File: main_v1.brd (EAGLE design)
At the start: 79.4 x 80.6 mm, 38 parts, among them IC1 MEGA8-P, IC2 7805TV, IC4 MC33063/MC34063P, IC5 MAX6921, IC6 MAX6921

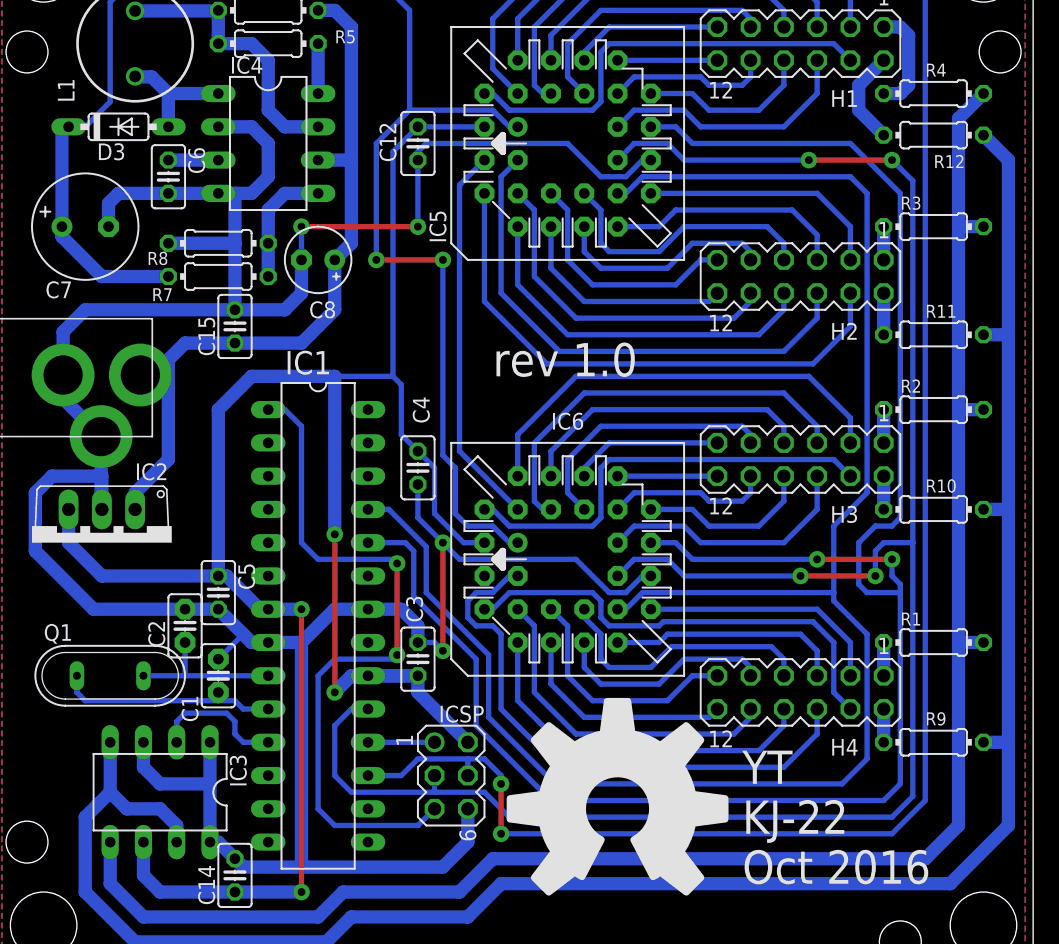
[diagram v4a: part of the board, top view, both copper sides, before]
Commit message: WIP Add a header for future expansion
Possible network connectivity, not sure how this is supposed to work
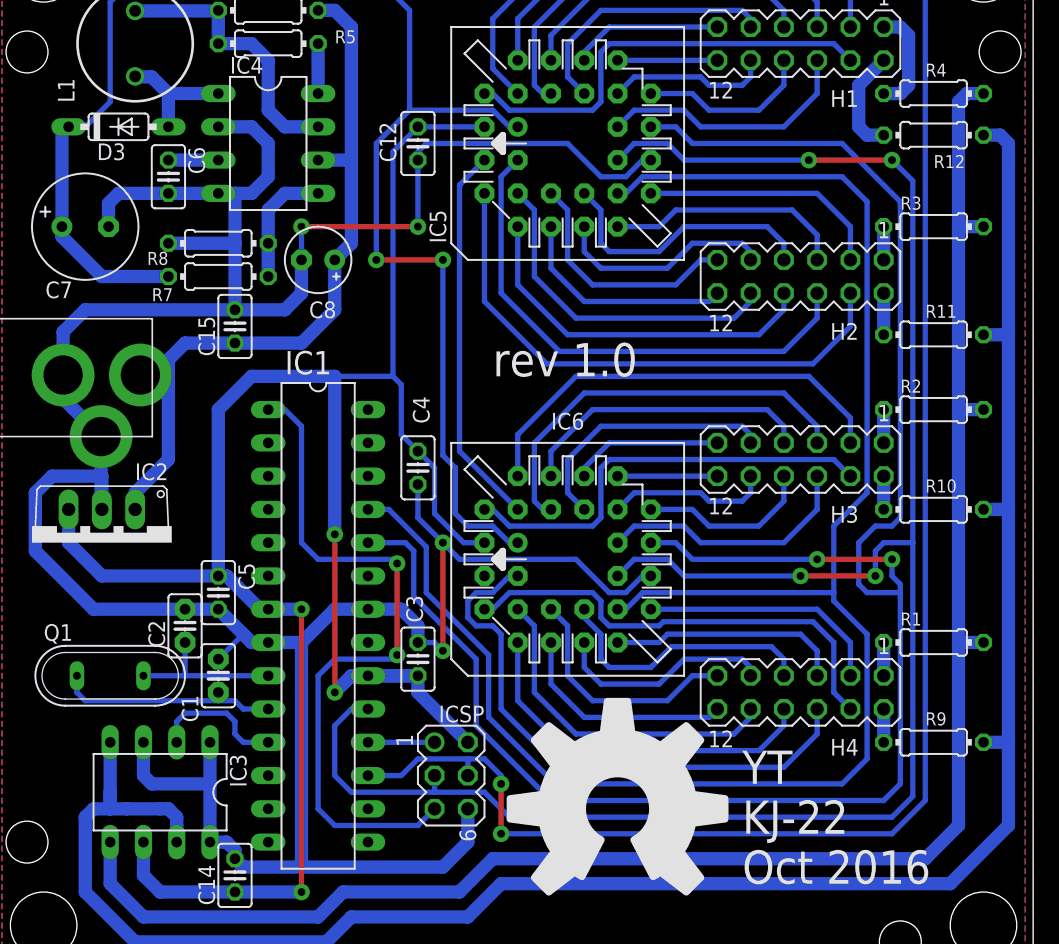
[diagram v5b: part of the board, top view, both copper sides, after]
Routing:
- net HT-: track 154.6 -> 157.2 mm
- net GND: track 249.1 -> 249.9 mm
- net HT-1: track 7.29 -> 8.04 mm
- net HT+: track 134.3 -> 135.0 mm
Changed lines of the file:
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@@
 <wire x1="26.035" y1="8.255" x2="21.59" y2="8.255" width="1.016" layer="16"/>
 <wire x1="21.59" y1="8.255" x2="20.955" y2="8.89" width="1.016" layer="16"/>
-<wire x1="20.955" y1="8.89" x2="19.685" y2="10.16" width="1.016" layer="16"/>
-<wire x1="19.685" y1="10.16" x2="19.05" y2="10.16" width="1.016" layer="16"/>
+<wire x1="20.955" y1="8.89" x2="20.955" y2="9.525" width="1.016" layer="16"/>
+<wire x1="20.955" y1="9.525" x2="20.32" y2="10.16" width="1.016" layer="16"/>
+<wire x1="20.32" y1="10.16" x2="19.05" y2="10.16" width="1.016" layer="16"/>
 <wire x1="19.05" y1="10.16" x2="19.05" y2="14.605" width="1.016" layer="16"/>
-<wire x1="19.05" y1="14.605" x2="15.24" y2="14.605" width="1.016" layer="16"/>
-<wire x1="15.24" y1="14.605" x2="13.97" y2="15.875" width="1.016" layer="16"/>
-<wire x1="13.97" y1="15.875" x2="13.97" y2="17.78" width="1.016" layer="16"/>
+<wire x1="19.05" y1="14.605" x2="14.605" y2="14.605" width="1.016" layer="16"/>
+<wire x1="14.605" y1="14.605" x2="13.97" y2="15.24" width="1.016" layer="16"/>
+<wire x1="13.97" y1="15.24" x2="13.97" y2="17.78" width="1.016" layer="16"/>
 <wire x1="19.05" y1="17.78" x2="19.05" y2="14.605" width="1.016" layer="16"/>
 <polygon width="0.4064" layer="16" spacing="10.16" isolate="1.016">
@@
 <wire x1="50.165" y1="59.69" x2="50.8" y2="59.69" width="0.4064" layer="16"/>
 <wire x1="50.8" y1="59.69" x2="52.07" y2="60.96" width="0.4064" layer="16"/>
-<wire x1="52.07" y1="60.96" x2="67.945" y2="60.96" width="0.4064" layer="16"/>
-<wire x1="67.945" y1="60.96" x2="69.215" y2="59.69" width="0.4064" layer="16"/>
-<wire x1="69.215" y1="59.69" x2="69.215" y2="36.83" width="0.4064" layer="16"/>
+<wire x1="52.07" y1="60.96" x2="67.31" y2="60.96" width="0.4064" layer="16"/>
+<wire x1="67.31" y1="60.96" x2="69.215" y2="59.055" width="0.4064" layer="16"/>
+<wire x1="69.215" y1="59.055" x2="69.215" y2="36.83" width="0.4064" layer="16"/>
 <wire x1="69.215" y1="36.83" x2="66.675" y2="34.29" width="0.4064" layer="16"/>
 <wire x1="66.675" y1="34.29" x2="66.675" y2="29.21" width="0.4064" layer="16"/>
@@
 <wire x1="52.705" y1="64.77" x2="54.61" y2="64.77" width="0.4064" layer="16"/>
 <wire x1="54.61" y1="64.77" x2="55.88" y2="63.5" width="0.4064" layer="16"/>
-<wire x1="55.88" y1="63.5" x2="67.945" y2="63.5" width="0.4064" layer="16"/>
-<wire x1="67.945" y1="63.5" x2="71.755" y2="59.69" width="0.4064" layer="16"/>
-<wire x1="71.755" y1="59.69" x2="71.755" y2="34.925" width="0.4064" layer="16"/>
+<wire x1="55.88" y1="63.5" x2="67.31" y2="63.5" width="0.4064" layer="16"/>
+<wire x1="67.31" y1="63.5" x2="71.755" y2="59.055" width="0.4064" layer="16"/>
+<wire x1="71.755" y1="59.055" x2="71.755" y2="34.925" width="0.4064" layer="16"/>
 <wire x1="71.755" y1="34.925" x2="71.12" y2="34.29" width="0.4064" layer="16"/>
 <wire x1="71.12" y1="34.29" x2="69.85" y2="34.29" width="0.4064" layer="16"/>
@@
 <contactref element="R12" pad="1"/>
 <wire x1="70.485" y1="69.85" x2="68.58" y2="67.945" width="1.016" layer="16"/>
-<wire x1="68.58" y1="67.945" x2="68.58" y2="66.04" width="1.016" layer="16"/>
-<wire x1="68.58" y1="66.04" x2="70.485" y2="64.135" width="1.016" layer="16"/>
+<wire x1="68.58" y1="67.945" x2="68.58" y2="64.77" width="1.016" layer="16"/>
+<wire x1="68.58" y1="64.77" x2="69.215" y2="64.135" width="1.016" layer="16"/>
+<wire x1="69.215" y1="64.135" x2="70.485" y2="64.135" width="1.016" layer="16"/>
 </signal>
 <signal name="HT-2">
@@
 <contactref element="R12" pad="2"/>
 <wire x1="11.43" y1="17.78" x2="11.43" y2="13.97" width="1.016" layer="16"/>
-<wire x1="11.43" y1="13.97" x2="12.7" y2="12.7" width="1.016" layer="16"/>
+<wire x1="11.43" y1="13.97" x2="11.43" y2="12.7" width="1.016" layer="16"/>
+<wire x1="11.43" y1="12.7" x2="12.7" y2="12.7" width="1.016" layer="16"/>
 <wire x1="12.7" y1="12.7" x2="15.24" y2="12.7" width="1.016" layer="16"/>
-<wire x1="15.24" y1="12.7" x2="16.51" y2="11.43" width="1.016" layer="16"/>
+<wire x1="15.24" y1="12.7" x2="15.875" y2="12.7" width="1.016" layer="16"/>
+<wire x1="15.875" y1="12.7" x2="16.51" y2="12.065" width="1.016" layer="16"/>
+<wire x1="16.51" y1="12.065" x2="16.51" y2="11.43" width="1.016" layer="16"/>
 <wire x1="16.51" y1="11.43" x2="16.51" y2="10.16" width="1.016" layer="16"/>
 <wire x1="75.565" y1="6.985" x2="41.275" y2="6.985" width="1.016" layer="16"/>
@@
 <wire x1="13.335" y1="2.54" x2="9.525" y2="6.35" width="1.016" layer="16"/>
 <wire x1="9.525" y1="6.35" x2="9.525" y2="12.065" width="1.016" layer="16"/>
-<wire x1="9.525" y1="12.065" x2="11.43" y2="13.97" width="1.016" layer="16"/>
+<wire x1="9.525" y1="12.065" x2="10.16" y2="12.7" width="1.016" layer="16"/>
+<wire x1="10.16" y1="12.7" x2="11.43" y2="12.7" width="1.016" layer="16"/>
+<wire x1="11.43" y1="12.7" x2="11.43" y2="13.97" width="1.016" layer="16"/>
 <wire x1="75.565" y1="6.985" x2="80.01" y2="11.43" width="1.016" layer="16"/>
 <wire x1="80.01" y1="11.43" x2="80.01" y2="17.78" width="1.016" layer="16"/>
@@
 <wire x1="80.01" y1="35.56" x2="80.01" y2="48.895" width="1.016" layer="16"/>
 <wire x1="80.01" y1="48.895" x2="80.01" y2="62.23" width="1.016" layer="16"/>
-<wire x1="80.01" y1="62.23" x2="78.105" y2="64.135" width="1.016" layer="16"/>
+<wire x1="80.01" y1="62.23" x2="80.01" y2="63.5" width="1.016" layer="16"/>
+<wire x1="80.01" y1="63.5" x2="79.375" y2="64.135" width="1.016" layer="16"/>
+<wire x1="79.375" y1="64.135" x2="78.105" y2="64.135" width="1.016" layer="16"/>
 <wire x1="78.105" y1="48.895" x2="80.01" y2="48.895" width="1.016" layer="16"/>
 <wire x1="78.105" y1="35.56" x2="80.01" y2="35.56" width="1.016" layer="16"/>
@@
 <wire x1="76.2" y1="43.18" x2="76.2" y2="57.15" width="1.016" layer="16"/>
 <wire x1="76.2" y1="57.15" x2="76.2" y2="65.405" width="1.016" layer="16"/>
-<wire x1="76.2" y1="65.405" x2="78.105" y2="67.31" width="1.016" layer="16"/>
+<wire x1="76.2" y1="65.405" x2="76.2" y2="66.675" width="1.016" layer="16"/>
+<wire x1="76.2" y1="66.675" x2="76.835" y2="67.31" width="1.016" layer="16"/>
+<wire x1="76.835" y1="67.31" x2="78.105" y2="67.31" width="1.016" layer="16"/>
 <wire x1="78.105" y1="57.15" x2="76.2" y2="57.15" width="1.016" layer="16"/>
 <wire x1="78.105" y1="43.18" x2="76.2" y2="43.18" width="1.016" layer="16"/>

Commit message: Prepare to move the atmega
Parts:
- added ESP8266: (no value), adafruit:2X04
- added ICSP2: (no value), con-lstb:MA05-1
- added R13, R14, R15, R16, R17: (no value), resistor:0204/7
- moved C4 0.63 mm to (34.9, 38.1)
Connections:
- new net N$10: ESP8266.1, ICSP2.1
- new net N$12: ESP8266.7, ICSP2.5, R17.2
- new net N$14: ESP8266.8, ICSP2.2
- new net N$17: ESP8266.3, R14.2
- new net N$19: ESP8266.5, R13.2
- new net SCL: ESP8266.4, IC1.28, R16.2
- new net SDA: ESP8266.6, IC1.27, ICSP2.4, R15.2
- net GND: now also ESP8266.2, ICSP2.3
- net VCC: now also R13.1, R14.1, R15.1, R16.1, R17.1
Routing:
- net VCC: track 169.1 -> 165.8 mm
- net N$1: track 29.3 -> 31.4 mm
- net VBB: track 114.2 -> 115.0 mm
- net GND: track 249.9 -> 249.2 mm

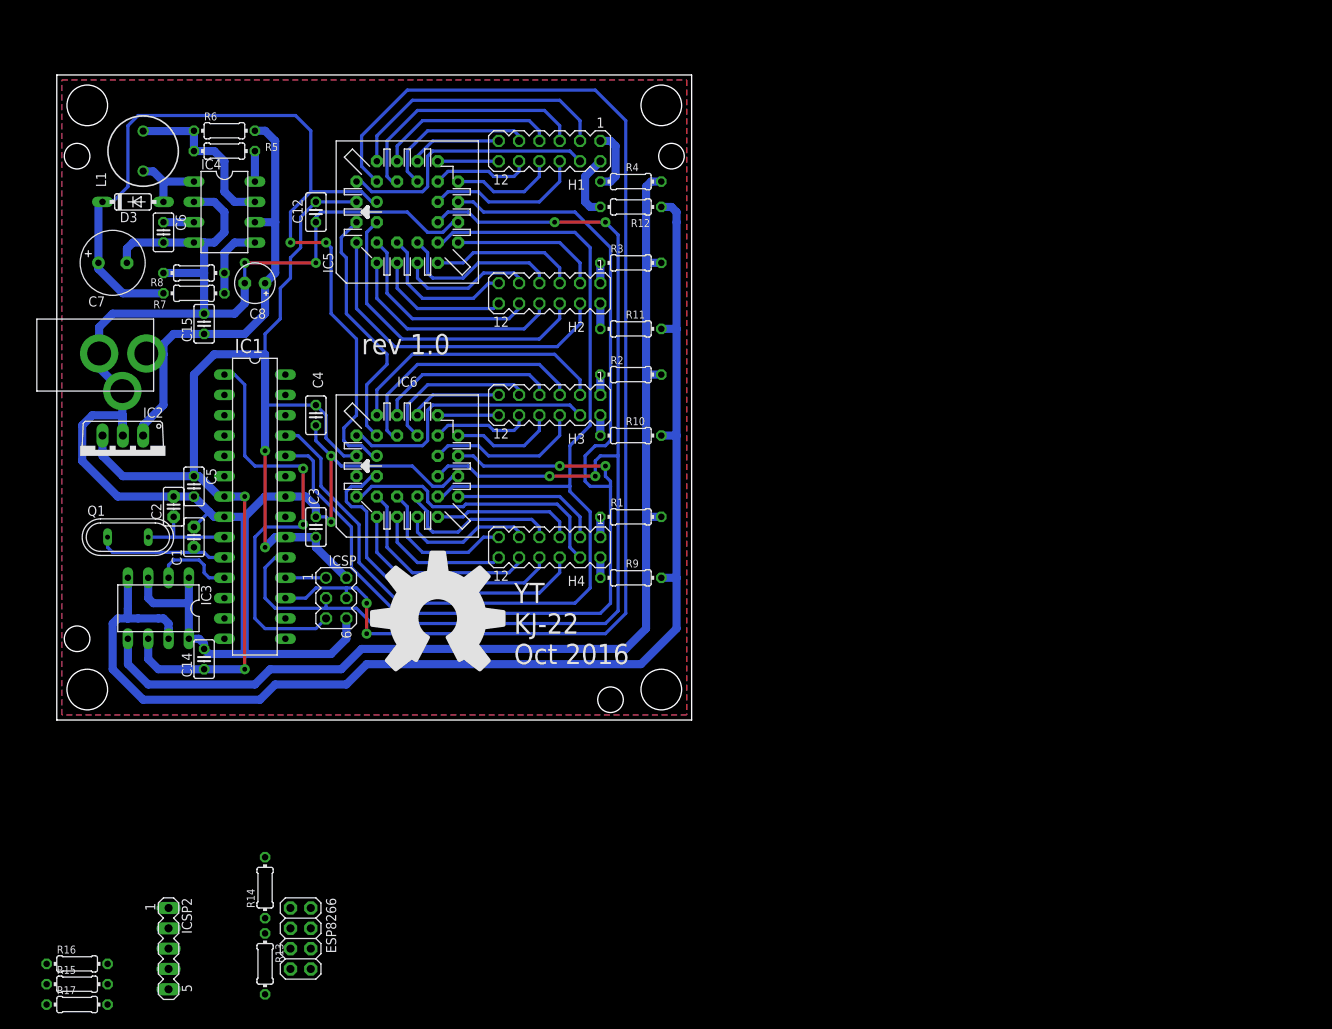
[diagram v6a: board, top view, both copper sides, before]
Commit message: Move ESP ICSP header, and bits into the board
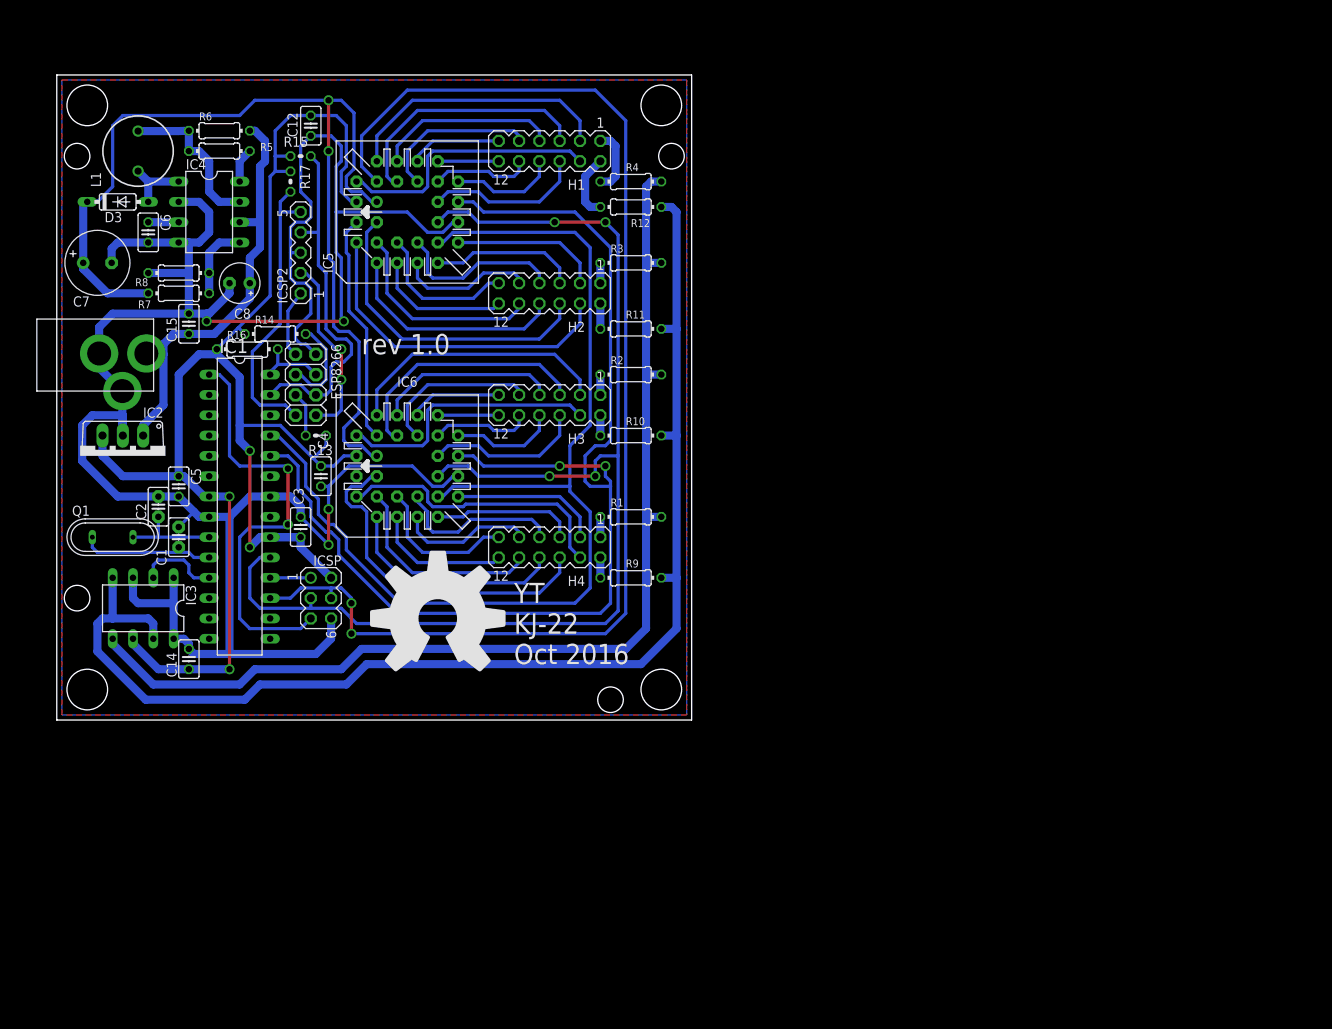
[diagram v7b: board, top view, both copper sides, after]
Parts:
- R13, R15, R17: device resistor:0204/7 -> resistor:0204V
- moved R15 107.2 mm to (33.0, 70.5)
- moved R17 106.3 mm to (31.8, 67.3), turned to 270 degrees
- moved ICSP2 88.5 mm to (33.0, 58.4), turned to 90 degrees
- moved R16 79.7 mm to (26.4, 46.4)
- moved R14 69.2 mm to (29.8, 48.3), turned to 0 degrees
- moved ESP8266 69.2 mm to (33.7, 41.9)
- moved R13 66.3 mm to (34.9, 35.6), turned to 180 degrees
- moved C12 10.8 mm to (34.3, 74.3)
- moved C4 7.65 mm to (35.6, 30.5)
- moved C8 1.91 mm to (25.4, 54.6)
- moved IC1 1.91 mm to (25.4, 26.7)
- moved IC4 1.91 mm to (21.6, 63.5)
- moved ICSP 1.91 mm to (35.6, 15.2)
- moved C7 1.91 mm to (7.62, 57.1)
- moved C2 1.90 mm to (15.2, 26.7)
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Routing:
- net GND: track 249.2 -> 304.2 mm
- net SDA: track 0.00 -> 44.8 mm
- net N$12: track 0.00 -> 36.5 mm
- net VCC: track 165.8 -> 195.6 mm
- net N$14: track 0.00 -> 23.4 mm, vias 0 -> 2
- net VBB: track 115.0 -> 127.5 mm
- net N$17: track 0.00 -> 11.7 mm
- net SCL: track 0.00 -> 8.86 mm
- net N$10: track 0.00 -> 8.52 mm
- net N$19: track 0.00 -> 5.61 mm
- net +5V: track 56.7 -> 53.3 mm
- net N$1: track 31.4 -> 28.8 mm
- net MOSI: track 155.4 -> 157.3 mm
- net SCK: track 151.3 -> 153.2 mm
- net N$8: track 21.4 -> 20.1 mm
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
